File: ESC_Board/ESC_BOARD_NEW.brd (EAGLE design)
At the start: 128.3 x 178 mm, 165 parts, among them J3 AVR_SPI_PROG_3X2NS, U1 FQB27P06, U2 ATMEGA328P_TQFP, U3 FQB27P06, U4 PCA9685

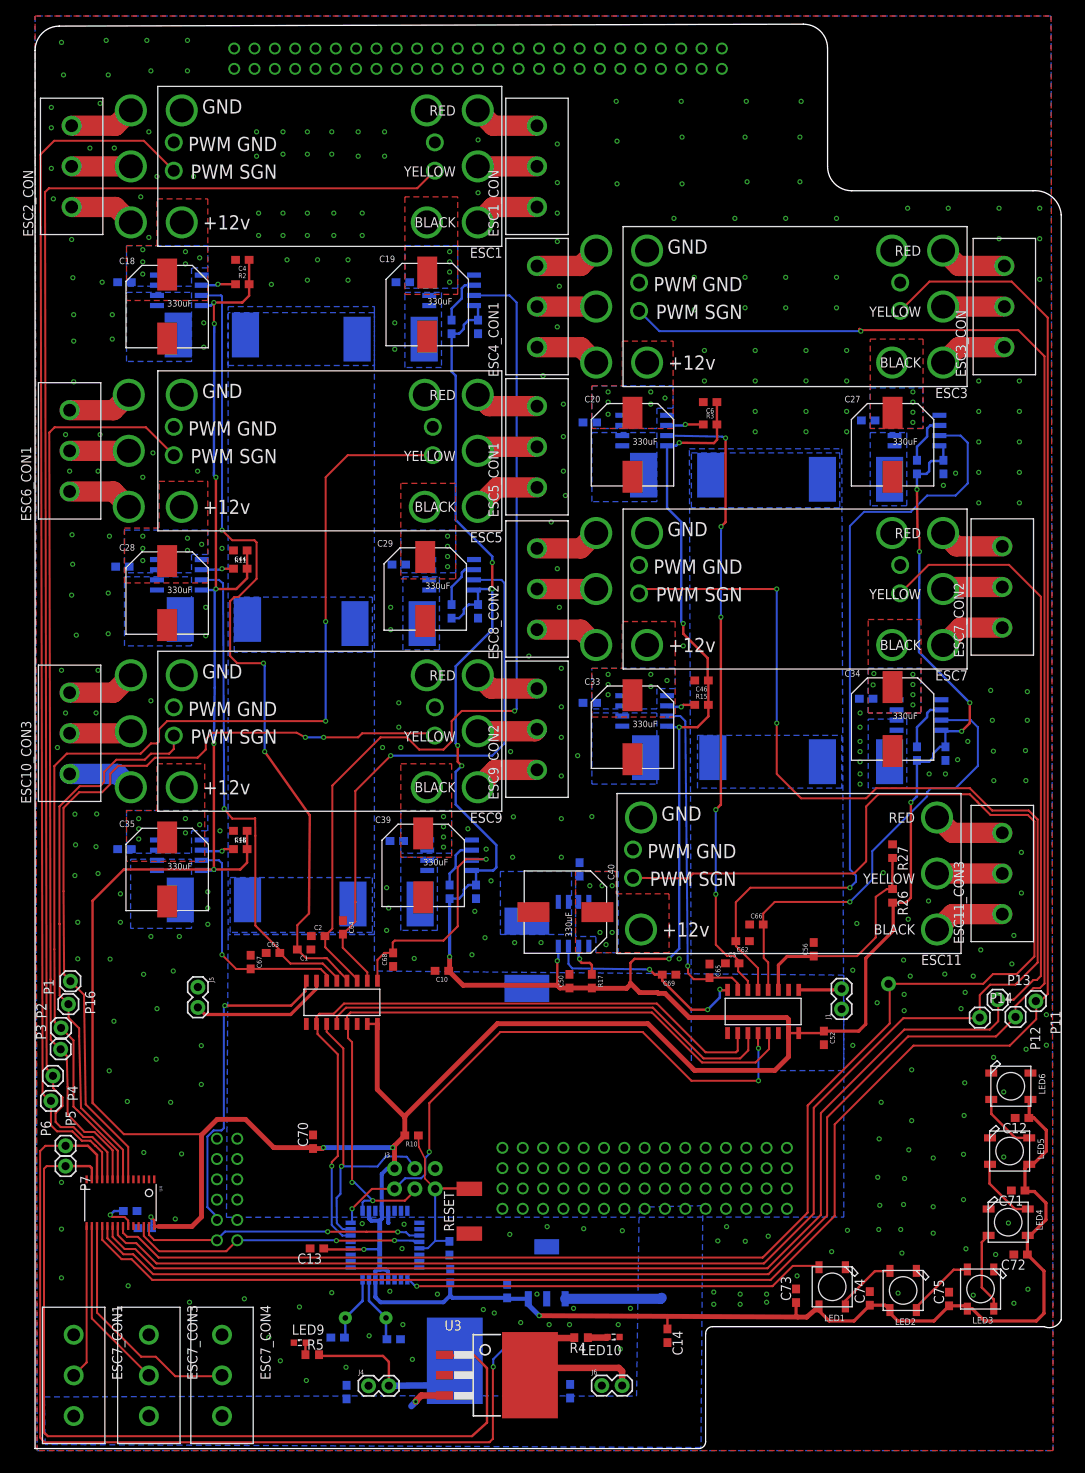
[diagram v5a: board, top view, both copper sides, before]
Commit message: Adding more test probes and cleaning up crooked traces
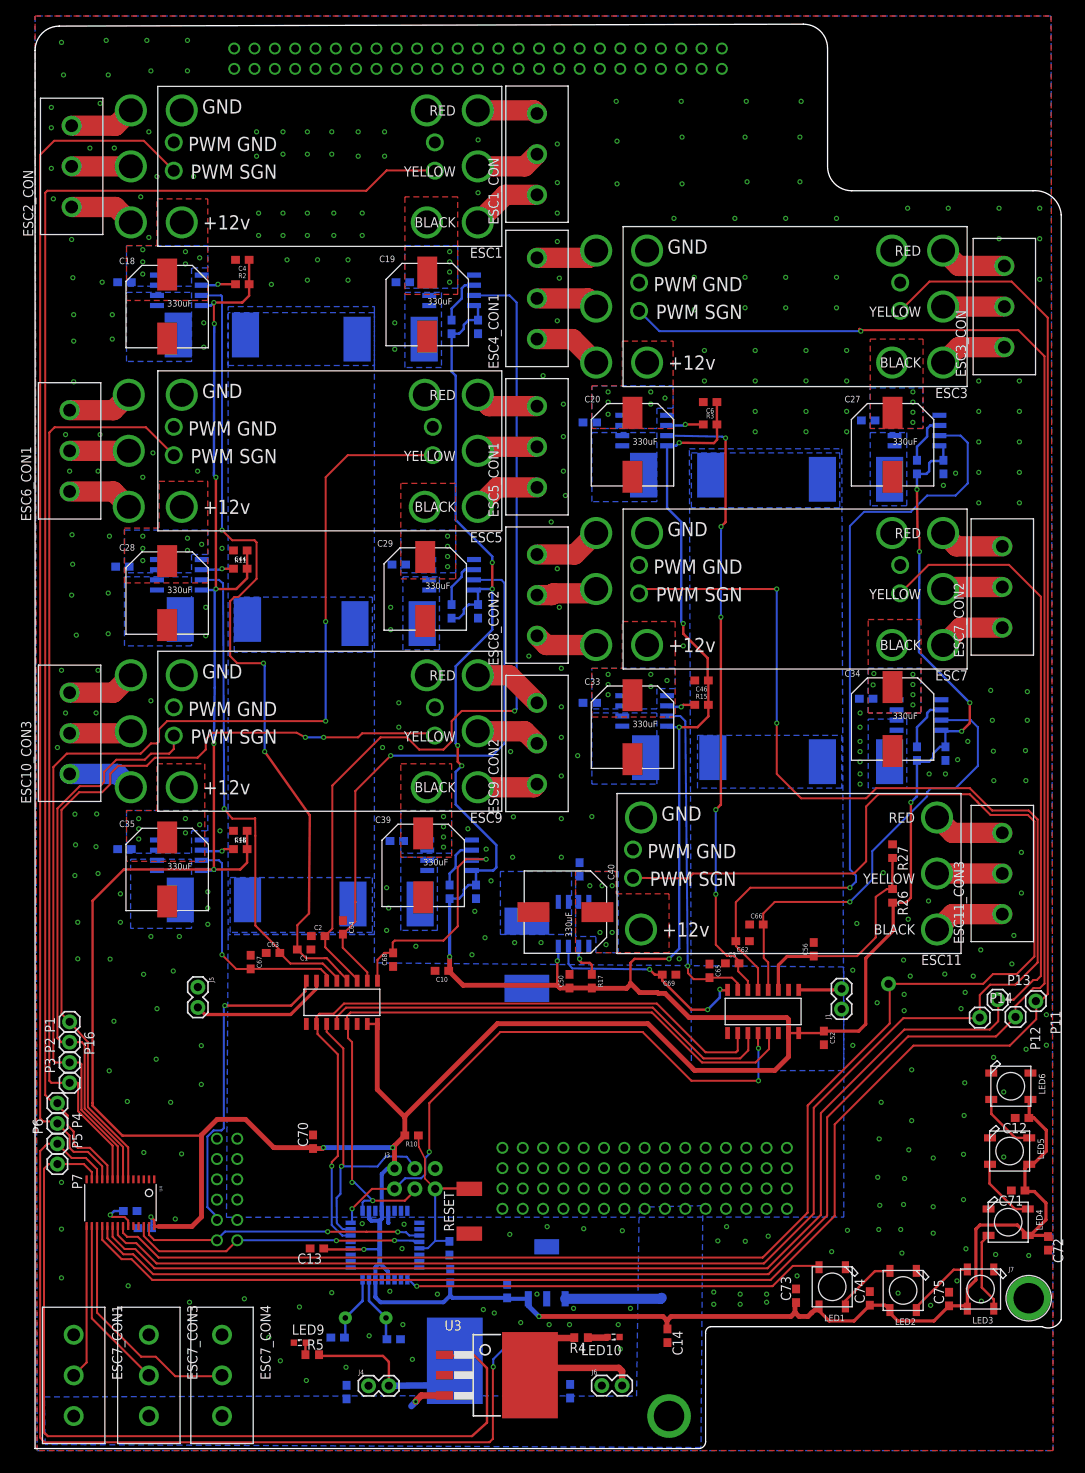
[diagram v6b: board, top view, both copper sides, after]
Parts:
- added J2, J7: (no value), SparkFun-Connectors:BANANA_CONN
- R10, R26, R27: value (none) -> 10k
- moved P16 5.08 mm to (4.32, 53.3)
- moved P1 4.75 mm to (4.32, 50.8)
- moved P2 4.45 mm to (4.32, 48.3)
- moved P3 4.34 mm to (4.32, 45.7)
- moved C72 3.70 mm to (126.6, 25.7), turned to 270 degrees
- moved P4 3.45 mm to (2.79, 43.2)
- moved P5 2.93 mm to (2.79, 40.6)
- moved ESC9_CON2 1.78 mm to (62.7, 88.1)
- moved ESC1_CON 1.52 mm to (62.7, 161.8)
- moved P6 1.05 mm to (2.79, 38.1)
- moved P7 1.05 mm to (2.79, 35.6)
- moved ESC4_CON1 1.02 mm to (62.7, 143.8)
- moved ESC8_CON2 0.76 mm to (62.7, 106.7)
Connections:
- net +12V: now also J2.P$1
- net GND: now also J7.P$1
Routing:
- net PWM6: track 137.1 -> 139.0 mm
- net PWM9: track 69.5 -> 71.3 mm
- net PWM5: track 114.5 -> 115.8 mm
- net PWM2: track 178.8 -> 177.6 mm
- net E_MAG_1_ON: track 120.6 -> 119.8 mm
- net N$33: track 8.30 -> 7.56 mm
- net N$31: track 8.09 -> 8.83 mm
- net N$9: track 8.20 -> 8.83 mm
- net N$8: track 7.40 -> 8.03 mm
- net N$7: track 8.20 -> 7.56 mm
- net +5V: track 793.5 -> 792.9 mm
- net N$32: track 7.51 -> 8.03 mm
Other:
- outline, holes or cut-outs redrawn

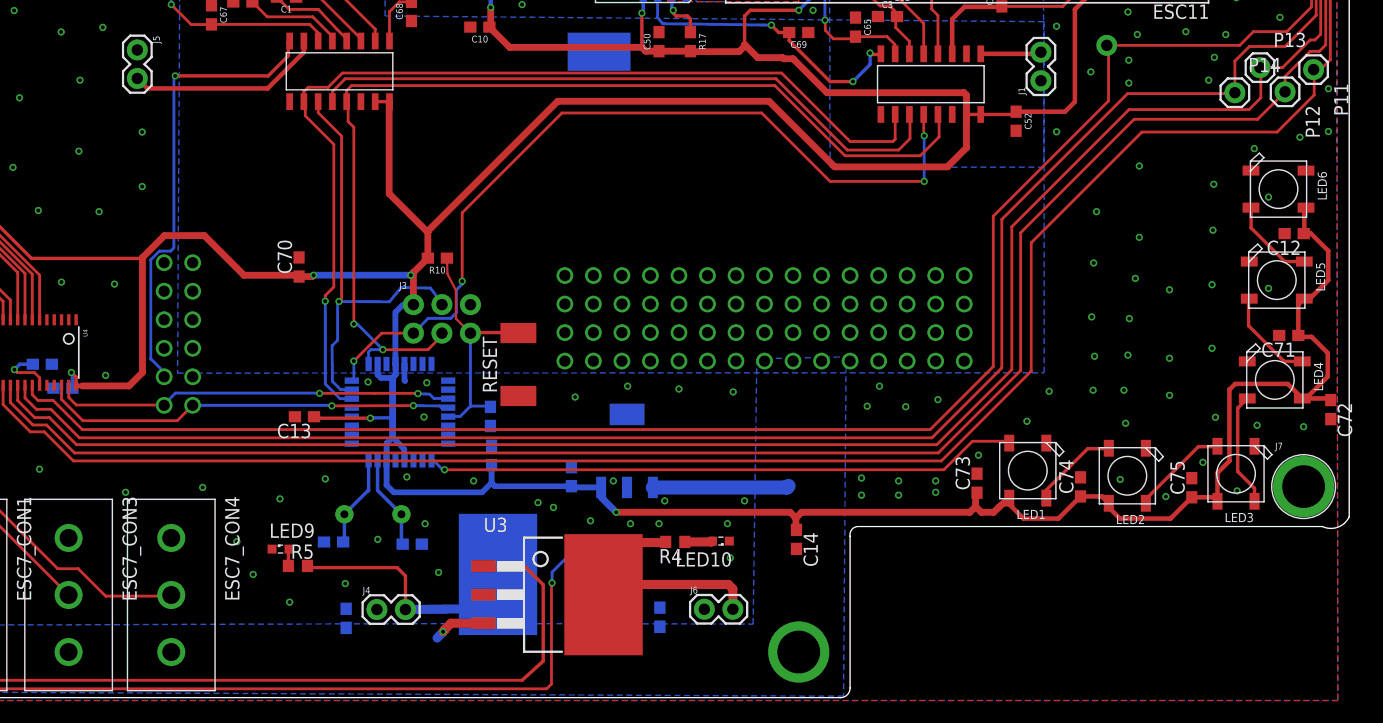
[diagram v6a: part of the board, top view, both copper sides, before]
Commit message: Fixed to work with new part
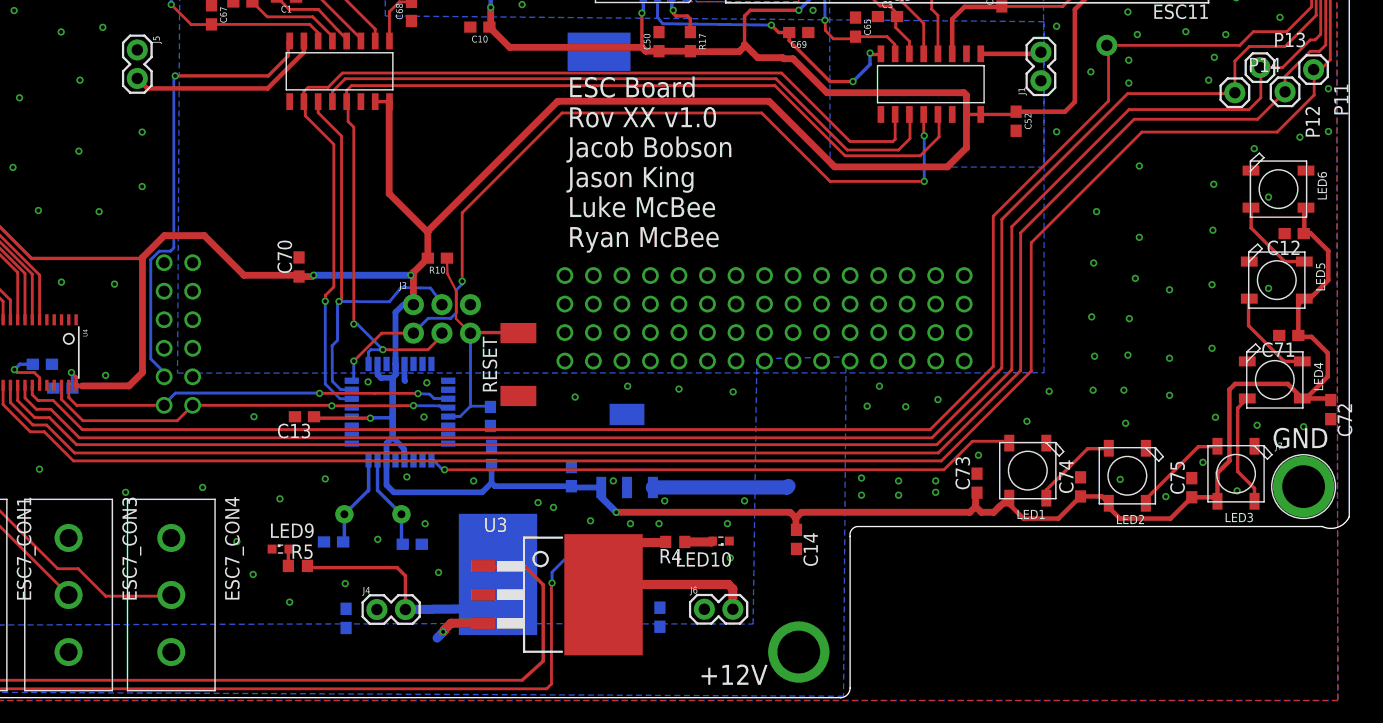
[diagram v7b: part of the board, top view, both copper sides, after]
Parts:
- removed U$14: ESC-CONNECTORPARALLELL, MotherboardParts:ESC-PARALLELL
- removed U$16: POWER_BRICK_CONNECTORS(2X6), MotherBoardParts2:POWER_BRICK_CONNECTORS(2X6)
- added U$15: ESC-FULL, MotherboardParts:ESC-FULL
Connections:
- net +12V: now also U$15.P$101, U$15.P$102, U$15.P$103, U$15.P$104, U$15.P$105, U$15.P$106, U$15.P$107, U$15.P$108, U$15.P$109, U$15.P$110, U$15.P$111, U$15.P$112, U$15.P$113, U$15.P$114, U$15.P$115, U$15.P$116, U$15.P$117, U$15.P$118, U$15.P$119, U$15.P$120, U$15.P$121, U$15.P$122, U$15.P$123, U$15.P$124, U$15.P$125, U$15.P$126, U$15.P$127, U$15.P$128, U$15.P$129, U$15.P$130, U$15.P$4, U$15.P$5, U$15.P$6, U$15.P$63, U$15.P$64, U$15.P$65, U$15.P$66, U$15.P$67, U$15.P$68, U$15.P$69, U$15.P$70, U$15.P$71, U$15.P$72, U$15.P$73, U$15.P$74, U$15.P$75, U$15.P$76, U$15.P$77, U$15.P$78, U$15.P$79, U$15.P$80, U$15.P$81, U$15.P$82, U$15.P$83, U$15.P$84, U$15.P$85, U$15.P$86, U$15.P$87, U$15.P$88, U$15.P$89, U$15.P$90, U$15.P$91, U$15.P$92; no longer U$14.P$101, U$14.P$102, U$14.P$103, U$14.P$104, U$14.P$105, U$14.P$106, U$14.P$107, U$14.P$108, U$14.P$109, U$14.P$110, U$14.P$111, U$14.P$112, U$14.P$113, U$14.P$114, U$14.P$115, U$14.P$116, U$14.P$117, U$14.P$118, U$14.P$119, U$14.P$120, U$14.P$121, U$14.P$122, U$14.P$123, U$14.P$124, U$14.P$125, U$14.P$126, U$14.P$127, U$14.P$128, U$14.P$129, U$14.P$130, U$14.P$51, U$14.P$52, U$14.P$53, U$14.P$54, U$14.P$55, U$14.P$56, U$14.P$57, U$14.P$58, U$14.P$59, U$14.P$60, U$14.P$61, U$14.P$62, U$14.P$63, U$14.P$64, U$14.P$65, U$14.P$66, U$14.P$67, U$14.P$68, U$14.P$69, U$14.P$70, U$14.P$71, U$14.P$72, U$14.P$73, U$14.P$74, U$14.P$75, U$14.P$76, U$14.P$77, U$14.P$78, U$14.P$79, U$14.P$80, U$16.P$7, U$16.P$8, U$16.P$9
- net 48_I_ANALOG: now also U$15.P$8; no longer U$16.P$5
- net GND: now also U$15.P$10, U$15.P$11, U$15.P$12, U$15.P$13, U$15.P$14, U$15.P$15, U$15.P$16, U$15.P$17, U$15.P$18, U$15.P$19, U$15.P$20, U$15.P$21, U$15.P$22, U$15.P$23, U$15.P$24, U$15.P$25, U$15.P$26, U$15.P$27, U$15.P$28, U$15.P$29, U$15.P$30, U$15.P$31, U$15.P$32, U$15.P$33, U$15.P$34, U$15.P$35, U$15.P$36, U$15.P$37, U$15.P$38, U$15.P$39, U$15.P$40, U$15.P$41, U$15.P$42, U$15.P$43, U$15.P$44, U$15.P$45, U$15.P$46, U$15.P$47, U$15.P$48, U$15.P$49, U$15.P$50, U$15.P$51, U$15.P$52, U$15.P$53, U$15.P$54, U$15.P$55, U$15.P$56, U$15.P$57, U$15.P$58, U$15.P$59, U$15.P$60, U$15.P$61, U$15.P$62; no longer U$14.P$1, U$14.P$10, U$14.P$11, U$14.P$12, U$14.P$13, U$14.P$14, U$14.P$15, U$14.P$16, U$14.P$17, U$14.P$18, U$14.P$19, U$14.P$2, U$14.P$20, U$14.P$21, U$14.P$22, U$14.P$23, U$14.P$24, U$14.P$25, U$14.P$26, U$14.P$27, U$14.P$28, U$14.P$29, U$14.P$3, U$14.P$30, U$14.P$31, U$14.P$32, U$14.P$33, U$14.P$34, U$14.P$35, U$14.P$36, U$14.P$37, U$14.P$38, U$14.P$39, U$14.P$4, U$14.P$40, U$14.P$41, U$14.P$42, U$14.P$43, U$14.P$44, U$14.P$45, U$14.P$46, U$14.P$47, U$14.P$48, U$14.P$49, U$14.P$5, U$14.P$50, U$14.P$6, U$14.P$7, U$14.P$8, U$14.P$9, U$16.P$1, U$16.P$2, U$16.P$3
- net SCL: now also U$15.P$1; no longer U$16.P$12
- net SDA: now also U$15.P$7; no longer U$16.P$6
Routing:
- net GND: vias 336 -> 337
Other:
- board text added: "+12V"
- board text added: "ESC Board Rov XX v1.0 Jacob Bobson Jason King Luke McBee Ryan McBee"
- board text added: "GND"

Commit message: Version submitted to elecrow
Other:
- board size 128.3 x 178 mm -> 128.3 x 177.8 mm
